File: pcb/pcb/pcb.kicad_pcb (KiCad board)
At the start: 2 copper layers, 90 x 70 mm, 76 parts, among them J1 Conn_01x03_Pin, J10 Conn_01x03_Pin, J11 Conn_01x03_Pin, J12 Conn_01x03_Pin, J13 Conn_01x03_Pin, J14 Conn_01x03_Pin, J15 Conn_01x03_Pin, J16 Conn_01x03_Pin, J17 Conn_01x03_Pin, J18 Conn_01x04_Pin, J2 Conn_01x03_Pin, J20 Conn_01x08_Socket, J3 Conn_01x03_Pin, J4 Conn_01x03_Pin, J5 Conn_01x03_Pin, J6 Conn_01x03_Pin, J7 Conn_01x03_Pin, J8 Conn_01x03_Pin, J9 Conn_01x03_Pin, U1 Pico, U2 4052, U3 4052, U4 LM324

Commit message: cleanup pcb
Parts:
- moved NT2 56.5 mm to (13.7, -11.7)
- moved C14 32.3 mm to (29.2, 40.8), turned to 90 degrees
- moved C1 19.0 mm to (-17.8, -7.11), turned to 180 degrees
- moved R32 18.0 mm to (-35.1, 21.3), turned to 180 degrees
- moved R31 14.7 mm to (-31.2, 21.3), turned to 180 degrees
- moved J17 10.7 mm to (-31.1, 5.84)
- moved JP1 10.7 mm to (-36.2, 8.37)
- moved J13 8.89 mm to (-15.2, 3.17)
- moved J14 8.89 mm to (-15.2, 6.99)
- moved J15 8.89 mm to (-15.2, 10.8)
- moved J16 8.89 mm to (-15.2, 14.6)
- moved J18 7.56 mm to (-27.4, 25.1), turned to -90 degrees
- moved J11 2.54 mm to (-15.2, 41.9)
- moved J12 2.54 mm to (15.2, 41.9)
- moved J3 2.54 mm to (-15.2, 34.3)
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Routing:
- net Net-(J5-Pin_3): track 86.3 -> 2.90 mm, vias 3 -> 0
- net Net-(J11-Pin_3): track 86.0 -> 2.90 mm, vias 3 -> 0
- net Net-(J6-Pin_3): track 75.1 -> 10.6 mm, vias 2 -> 0
- net Net-(J12-Pin_3): track 66.7 -> 2.90 mm, vias 1 -> 0
- net Net-(J3-Pin_3): track 59.5 -> 2.90 mm, vias 3 -> 0
- net Net-(J9-Pin_3): track 53.9 -> 2.90 mm, vias 1 -> 0
- net Net-(J7-Pin_3): track 50.6 -> 2.90 mm, vias 1 -> 0
- net Net-(J4-Pin_3): track 40.1 -> 2.90 mm, vias 1 -> 0
- net Net-(J1-Pin_3): track 34.7 -> 2.90 mm, vias 2 -> 0
- net +5VP: track 156.5 -> 170.2 mm
- net GND: track 46.2 -> 56.9 mm
- net ext2: track 22.0 -> 13.1 mm
- net ext3: track 23.3 -> 14.4 mm
- net ext1: track 23.3 -> 14.4 mm
- net ext4: track 22.0 -> 13.1 mm
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
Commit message: cleanup pcb2
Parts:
- renumbered REF** to Hole1, REF** to Hole2, REF** to Hole3, REF** to Hole4
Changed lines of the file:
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@@
     (tags "mounting hole 3.2mm no annular m3")
     (attr exclude_from_pos_files exclude_from_bom)
-    (fp_text reference "REF**" (at 0 -4.2) (layer "F.SilkS") hide
+    (fp_text reference "Hole4" (at 0 -4.2) (layer "F.SilkS") hide
         (effects (font (size 1 1) (thickness 0.15)))
     )
@@
     (tags "mounting hole 3.2mm no annular m3")
     (attr exclude_from_pos_files exclude_from_bom)
-    (fp_text reference "REF**" (at 0 -4.2) (layer "F.SilkS") hide
+    (fp_text reference "Hole1" (at 0 -4.2) (layer "F.SilkS") hide
         (effects (font (size 1 1) (thickness 0.15)))
     )
@@
     (tags "mounting hole 3.2mm no annular m3")
     (attr exclude_from_pos_files exclude_from_bom)
-    (fp_text reference "REF**" (at 0 -4.2) (layer "F.SilkS") hide
+    (fp_text reference "Hole2" (at 0 -4.2) (layer "F.SilkS") hide
         (effects (font (size 1 1) (thickness 0.15)))
     )
@@
     (tags "mounting hole 3.2mm no annular m3")
     (attr exclude_from_pos_files exclude_from_bom)
-    (fp_text reference "REF**" (at 0 -4.2) (layer "F.SilkS") hide
+    (fp_text reference "Hole3" (at 0 -4.2) (layer "F.SilkS") hide
         (effects (font (size 1 1) (thickness 0.15)))
     )

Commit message: autoroute
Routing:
- net GND: track 56.9 -> 346.0 mm, vias 0 -> 4
- net +5V: track 1.91 -> 130.1 mm, vias 0 -> 3
- net Net-(J5-Pin_3): track 2.90 -> 110.8 mm, vias 0 -> 1
- net GNDPWR: track 138.8 -> 214.1 mm, vias 0 -> 2
- net Net-(J11-Pin_3): track 2.90 -> 77.5 mm, vias 0 -> 1
- net Net-(J1-Pin_3): track 2.90 -> 69.3 mm, vias 0 -> 1
- net Net-(J6-Pin_3): track 10.6 -> 75.3 mm, vias 0 -> 1
- net Net-(J12-Pin_3): track 2.90 -> 64.9 mm, vias 0 -> 1
- net ultrason_trig: track 0.00 -> 60.8 mm, vias 0 -> 2
- net ultrason_echo: track 1.98 -> 61.7 mm, vias 0 -> 2
- net Net-(U2-Y): track 0.00 -> 52.7 mm
- net uart_tx: track 0.00 -> 52.4 mm, vias 0 -> 1
- net Net-(J9-Pin_3): track 2.90 -> 54.7 mm, vias 0 -> 3
- net Net-(J3-Pin_3): track 2.90 -> 54.7 mm, vias 0 -> 1
- net Net-(J7-Pin_3): track 2.90 -> 50.7 mm, vias 0 -> 1
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- added copper zone on B.Cu, net GND
- added copper zone on F.Cu, net GND

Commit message: Final PCB revision, i guess?
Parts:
- added C15: C, Capacitor_SMD:C_0805_2012Metric, F.Cu at (-20.0, -13.3)
- added C16: C, Capacitor_SMD:C_0805_2012Metric, F.Cu at (-20.0, 31.1)
- added C17: C, Capacitor_SMD:C_0805_2012Metric, F.Cu at (24.1, 31.9)
- added C18: C, Capacitor_SMD:C_0805_2012Metric, F.Cu at (-19.1, 17.8)
- added C19: C, Capacitor_SMD:C_0805_2012Metric, B.Cu at (14.5, -12.6)
- added C20: C, Capacitor_SMD:C_0805_2012Metric, F.Cu at (-31.5, 28.3)
- added C21: C, Capacitor_SMD:C_0805_2012Metric, B.Cu at (24.5, 19.0)
- added C22: C, Capacitor_SMD:C_0805_2012Metric, F.Cu at (12.1, 27.4)
- added C23: C, Capacitor_SMD:C_0805_2012Metric, B.Cu at (28.7, -16.9)
- added C24: C, Capacitor_SMD:C_0805_2012Metric, B.Cu at (21.3, 1.78)
- added NT3: NetTie_2, NetTie:NetTie-2_SMD_Pad0.5mm, F.Cu at (-12.2, -18.4)
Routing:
- net GND: track 346.0 -> 585.6 mm, vias 4 -> 16
- net GNDPWR: track 214.1 -> 262.5 mm, vias 2 -> 13
- net +5V: track 130.1 -> 155.2 mm
- net +5VP: track 170.7 -> 184.7 mm
- added copper zone on B.Cu, net GNDPWR
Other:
- board text added: "+5V"
- board text added: "CD4052"
- board text added: "Echo"
- board text added: "GND"
- board text added: "GP12"
- board text added: "GP13"
- board text added: "GP14"
- board text added: "GP15"
- board text added: "GP16 TX"
- board text added: "GP17 RX"
- board text added: "GY-521 (MPU6050)"
- board text added: "JLCJLCJLCJLC"
- board text added: "Knee"
- board text added: "LM324"
- board text added: "Mid"
- board text added: "Middle"
- board text added: "Raspi Pico"
- board text added: "Trig"
- board text added: "UART"
- board text added: "Ultrasonic (HC-SR04)"
- board text added: "Upper"
- board text added: "auxiliary servos"
- board text added: "https://github.com/Windfisch/robocat TODO REVISION"
- board text added: "meow"
- board text added: "x"
- board text added: "y"
- board text added: "z=up"

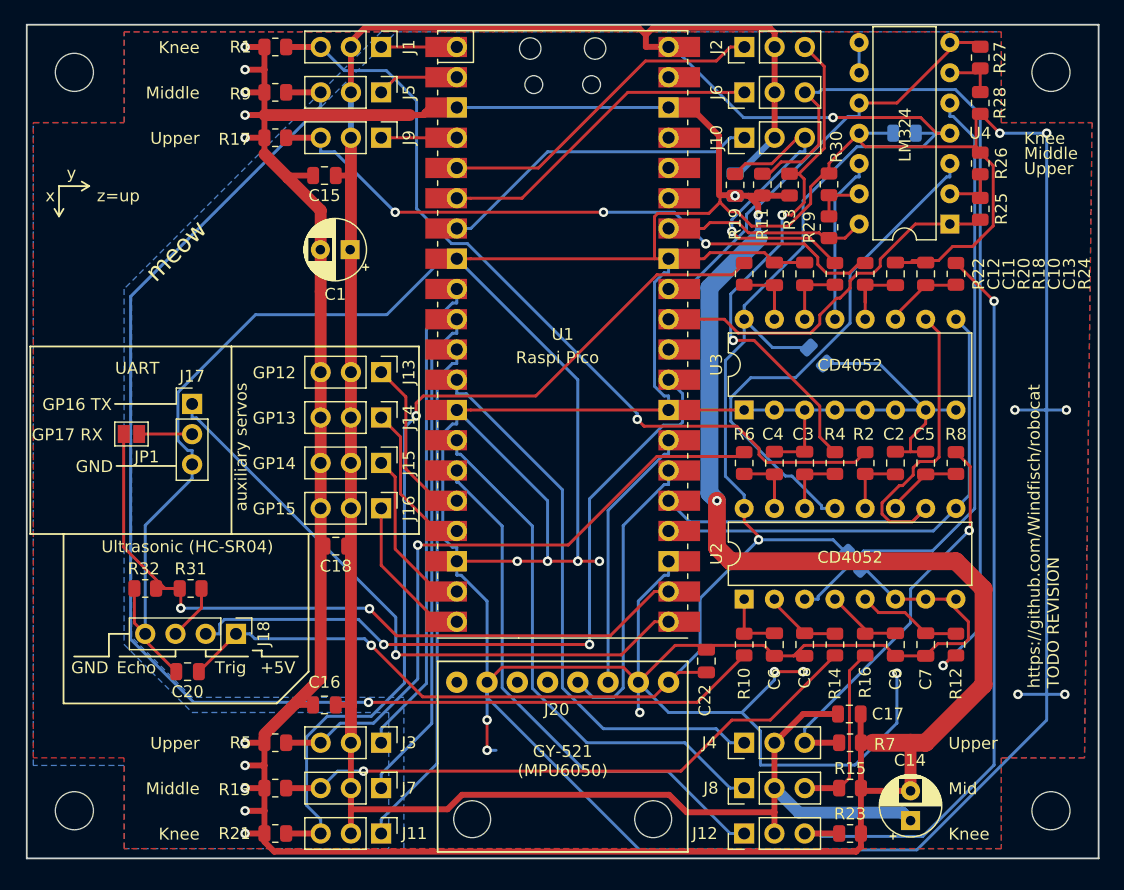
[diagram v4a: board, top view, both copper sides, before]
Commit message: fillet corners
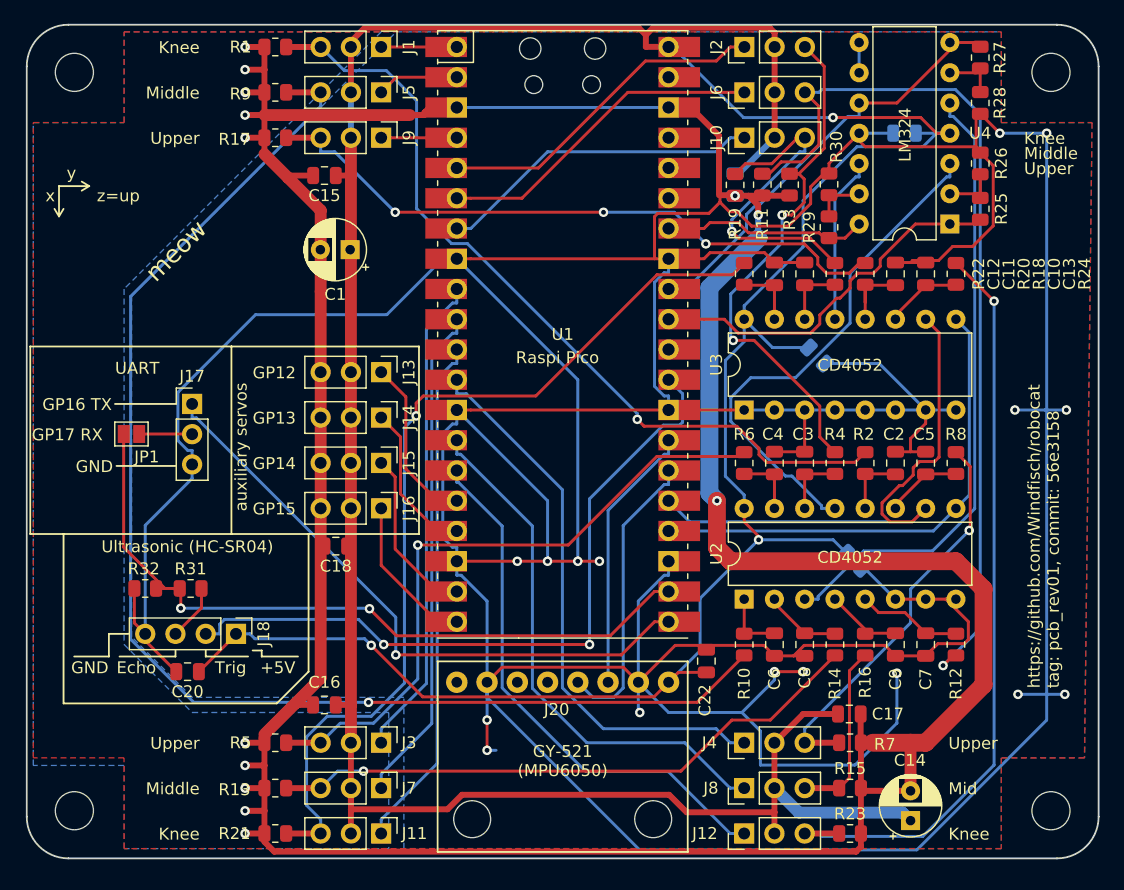
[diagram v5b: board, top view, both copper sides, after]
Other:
- outline, holes or cut-outs redrawn
- board text added: "https://github.com/Windfisch/robocat tag: pcb_rev01, commit: 56e3158"
- board text removed: "https://github.com/Windfisch/robocat TODO REVISION"
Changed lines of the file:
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@@
 			(outputformat 1)
 			(mirror no)
-			(drillshape 1)
+			(drillshape 0)
 			(scaleselection 1)
-			(outputdirectory "")
+			(outputdirectory "fab/")
 		)
 	)
@@
 			)
 			(layer "F.CrtYd")
-			(net 129)
+			(net 128)
 		)
 		(fp_line
@@
 		(layer "F.SilkS")
 	)
-	(gr_rect
-		(start -45 -26)
-		(end 45 44)
-		(locked yes)
+	(gr_line
+		(start 45 -22.5)
+		(end 45 40.5)
+		(stroke
+			(width 0.15)
+			(type default)
+		)
+		(layer "Edge.Cuts")
+	)
+	(gr_line
+		(start 41.5 44)
+		(end -41.5 44)
+		(stroke
+			(width 0.15)
+			(type default)
+		)
+		(layer "Edge.Cuts")
+	)
+	(gr_line
+		(start -45 40.5)
+		(end -45 -22.5)
+		(stroke
+			(width 0.15)
+			(type default)
+		)
+		(layer "Edge.Cuts")
+	)
+	(gr_arc
+		(start 45 40.5)
+		(mid 43.974874 42.974874)
+		(end 41.5 44)
+		(stroke
+			(width 0.15)
+			(type default)
+		)
+		(layer "Edge.Cuts")
+	)
+	(gr_arc
+		(start -41.5 44)
+		(mid -43.974874 42.974874)
+		(end -45 40.5)
+		(stroke
+			(width 0.15)
+			(type default)
+		)
+		(layer "Edge.Cuts")
+	)
+	(gr_arc
+		(start 41.5 -26)
+		(mid 43.974874 -24.974874)
+		(end 45 -22.5)
+		(stroke
+			(width 0.15)
+			(type default)
+		)
+		(layer "Edge.Cuts")
+	)
+	(gr_arc
+		(start -45 -22.5)
+		(mid -43.974874 -24.974874)
+		(end -41.5 -26)
+		(stroke
+			(width 0.15)
+			(type default)
+		)
+		(layer "Edge.Cuts")
+	)
+	(gr_line
+		(start -41.5 -26)
+		(end 41.5 -26)
 		(stroke
 			(width 0.15)
 			(type default)
 		)
-		(fill none)
 		(layer "Edge.Cuts")
 	)
@@
 		)
 	)
-	(gr_text "https://github.com/Windfisch/robocat\nTODO REVISION"
+	(gr_text "https://github.com/Windfisch/robocat\ntag: pcb_rev01, commit: 56e3158"
 		(at 41.783 29.718 90)
 		(layer "F.SilkS")

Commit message: final pcb rev01
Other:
- board text added: "https://github.com/Windfisch/robocat tag: pcb_rev01, commit: 64d77e1"
- board text removed: "https://github.com/Windfisch/robocat tag: pcb_rev01, commit: 56e3158"
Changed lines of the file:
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@@
 			)
 			(layer "F.CrtYd")
-			(net 128)
+			(net 129)
 		)
 		(fp_line
@@
 		)
 	)
-	(gr_text "https://github.com/Windfisch/robocat\ntag: pcb_rev01, commit: 56e3158"
+	(gr_text "https://github.com/Windfisch/robocat\ntag: pcb_rev01, commit: 64d77e1"
 		(at 41.783 29.718 90)
 		(layer "F.SilkS")
